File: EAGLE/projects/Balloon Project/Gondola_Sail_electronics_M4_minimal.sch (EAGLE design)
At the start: 38 parts

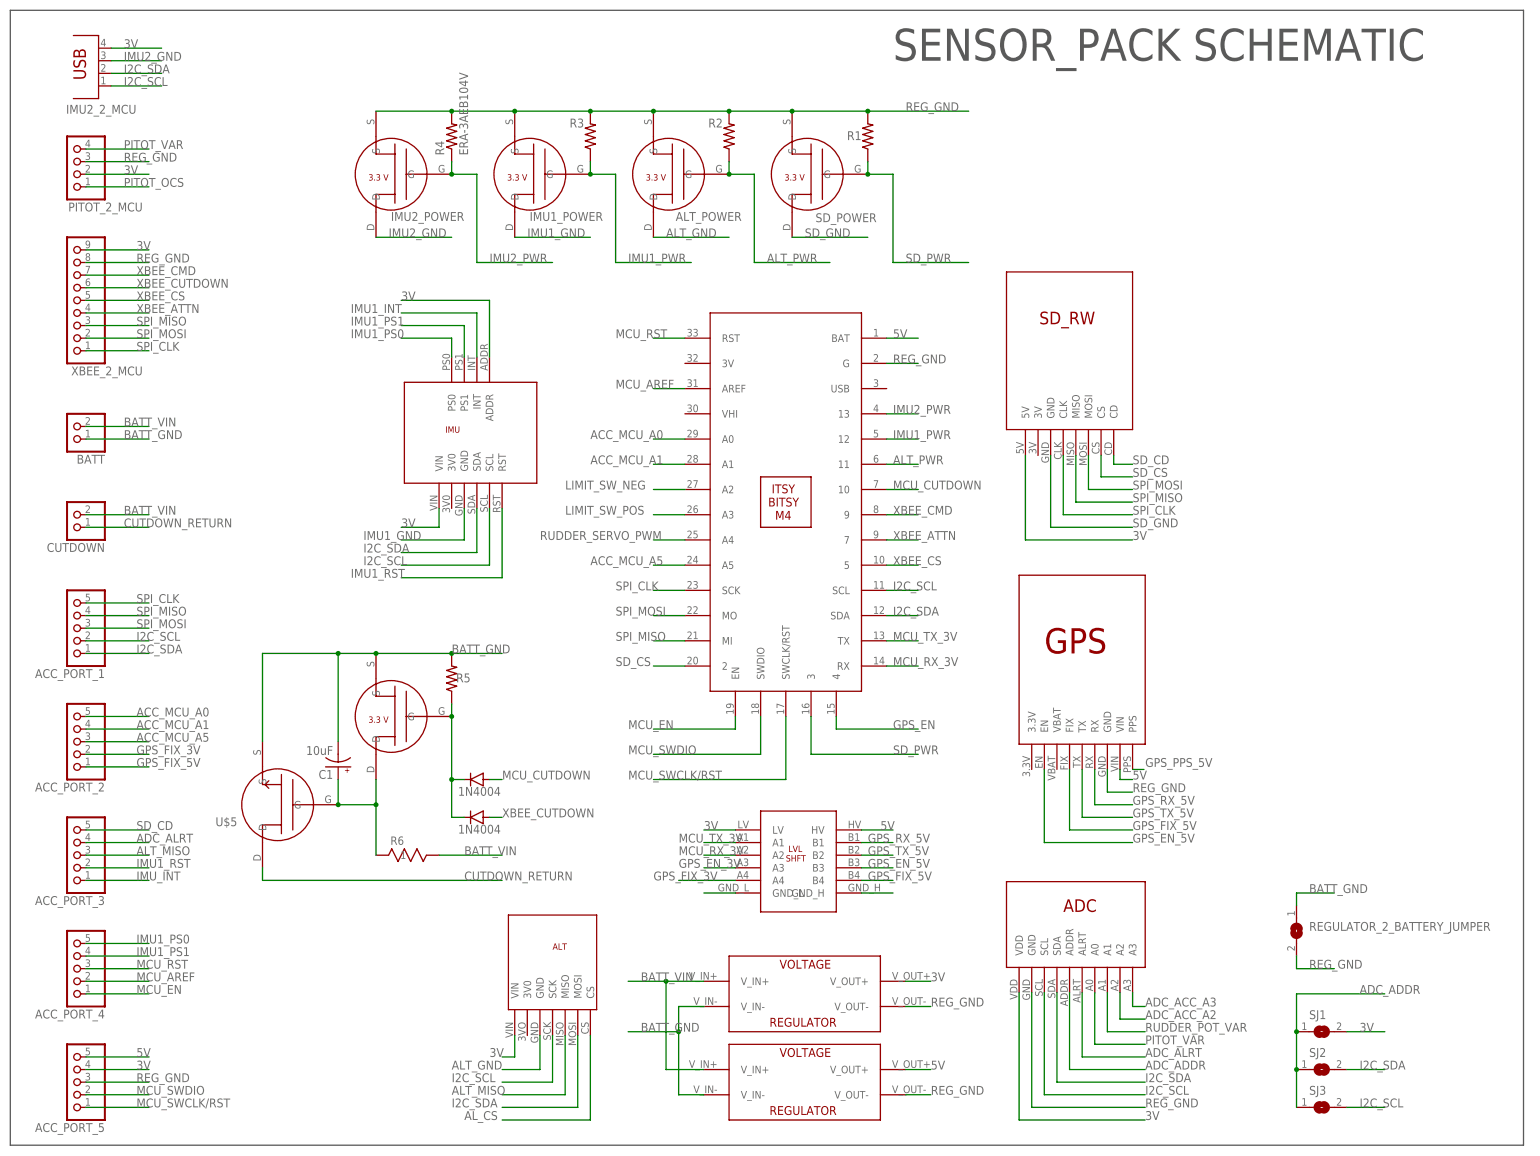
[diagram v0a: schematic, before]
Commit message: added minimal sensorpack
full sensor pack has too many breakout pins, need to trim down the size of the board. starting routing traces
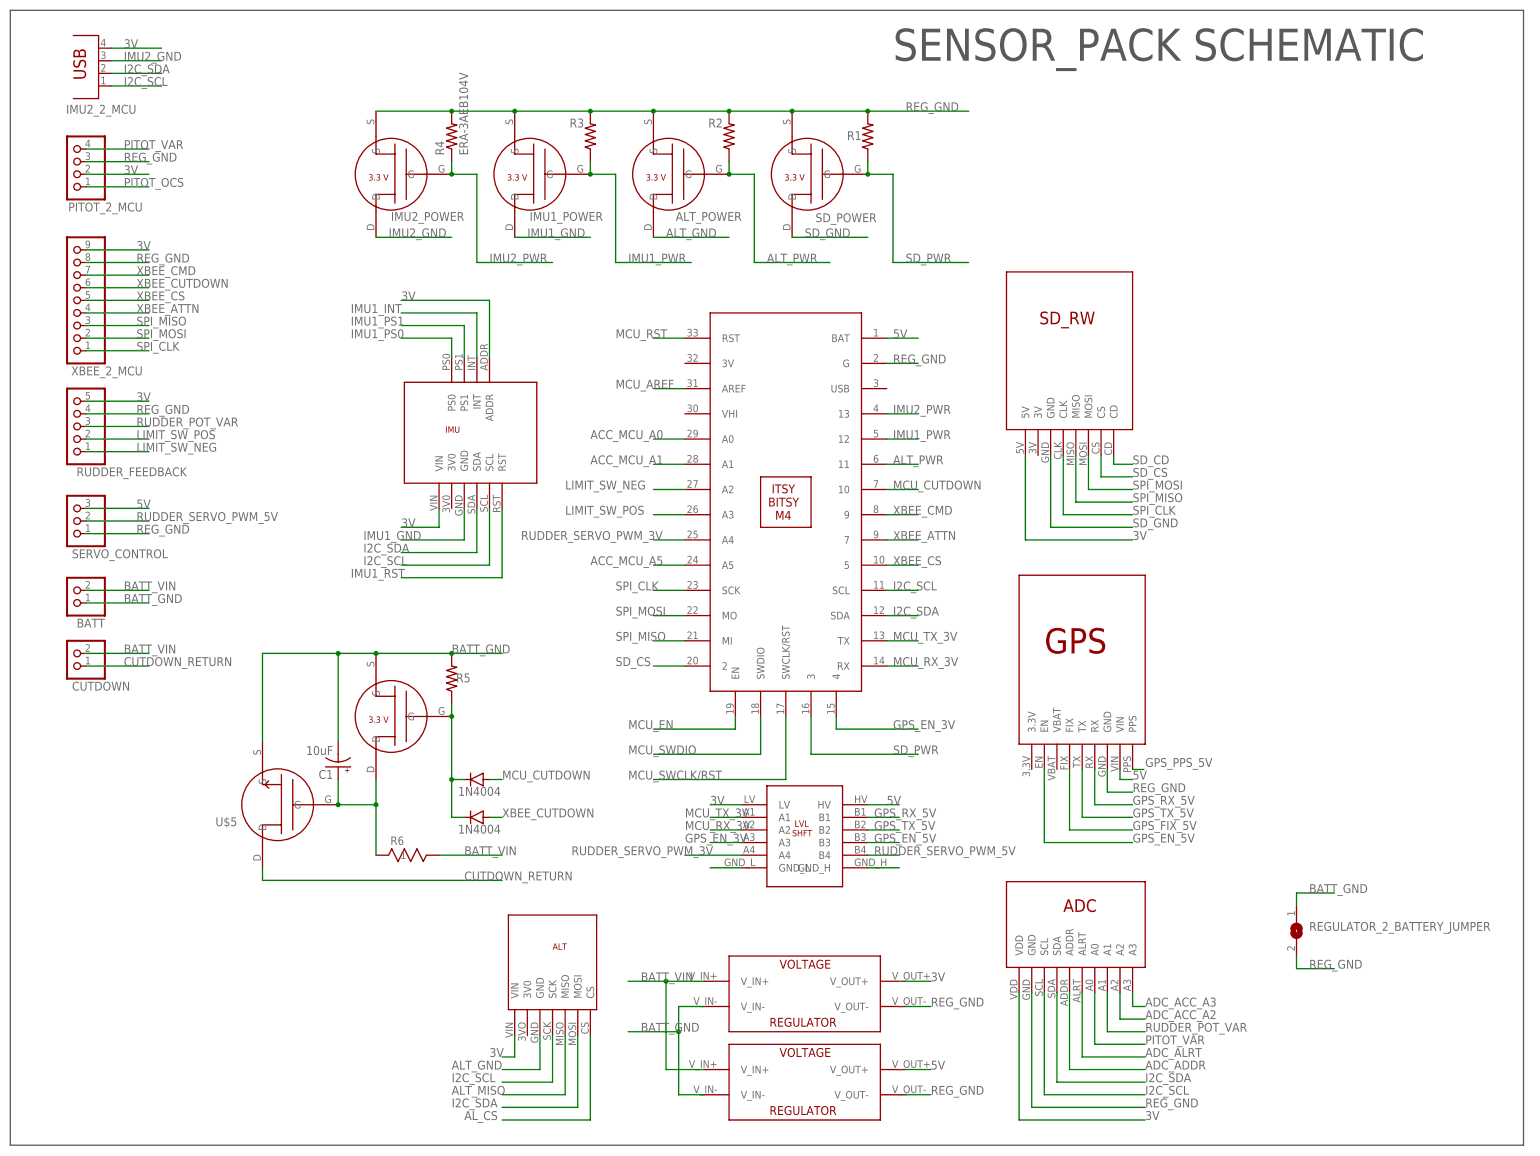
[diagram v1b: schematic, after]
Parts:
- removed ACC_PORT_1, ACC_PORT_2, ACC_PORT_3, ACC_PORT_4, ACC_PORT_5: (no value), pinhead:PINHD-1X5/90
- removed SJ1, SJ2, SJ3: (no value), jumper:SJ
- added RUDDER_FEEDBACK: (no value), pinhead:PINHD-1X5/90
- added SERVO_CONTROL: (no value), pinhead:PINHD-1X3/90
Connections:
- removed net GPS_EN: U$8.4
- removed net GPS_FIX_3V: ACC_PORT_2.2, U$6.A4
- removed net IMU_INT: ACC_PORT_3.1
- removed net RUDDER_SERVO_PWM: U$8.A4
- new net RUDDER_SERVO_PWM_3V: U$6.A4, U$8.A4
- new net RUDDER_SERVO_PWM_5V: SERVO_CONTROL.2, U$6.B4
- net 3V: now also RUDDER_FEEDBACK.5; no longer ACC_PORT_5.4, SJ1.2
- net 5V: now also SERVO_CONTROL.3; no longer ACC_PORT_5.5
- net ACC_MCU_A0: no longer ACC_PORT_2.5
- net ACC_MCU_A1: no longer ACC_PORT_2.4
- net ACC_MCU_A5: no longer ACC_PORT_2.3
- net ADC_ADDR: no longer SJ1.1, SJ2.1, SJ3.1
- net ADC_ALRT: no longer ACC_PORT_3.4
- net ALT_MISO: no longer ACC_PORT_3.3
- net GPS_EN_3V: now also U$8.4
- net GPS_FIX_5V: no longer ACC_PORT_2.1, U$6.B4
- net I2C_SCL: no longer ACC_PORT_1.2, SJ3.2
- net I2C_SDA: no longer ACC_PORT_1.1, SJ2.2
- net IMU1_PS0: no longer ACC_PORT_4.5
- net IMU1_PS1: no longer ACC_PORT_4.4
- net IMU1_RST: no longer ACC_PORT_3.2
- net LIMIT_SW_NEG: now also RUDDER_FEEDBACK.1
- net LIMIT_SW_POS: now also RUDDER_FEEDBACK.2
- net MCU_AREF: no longer ACC_PORT_4.2
- net MCU_EN: no longer ACC_PORT_4.1
- net MCU_RST: no longer ACC_PORT_4.3
- net MCU_SWCLK/RST: no longer ACC_PORT_5.1
- net MCU_SWDIO: no longer ACC_PORT_5.2
- net REG_GND: now also RUDDER_FEEDBACK.4, SERVO_CONTROL.1; no longer ACC_PORT_5.3
- net RUDDER_POT_VAR: now also RUDDER_FEEDBACK.3
- net SD_CD: no longer ACC_PORT_3.5
- net SPI_CLK: no longer ACC_PORT_1.5
- net SPI_MISO: no longer ACC_PORT_1.4
- net SPI_MOSI: no longer ACC_PORT_1.3
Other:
- moved on the sheet: BATT, CUTDOWN

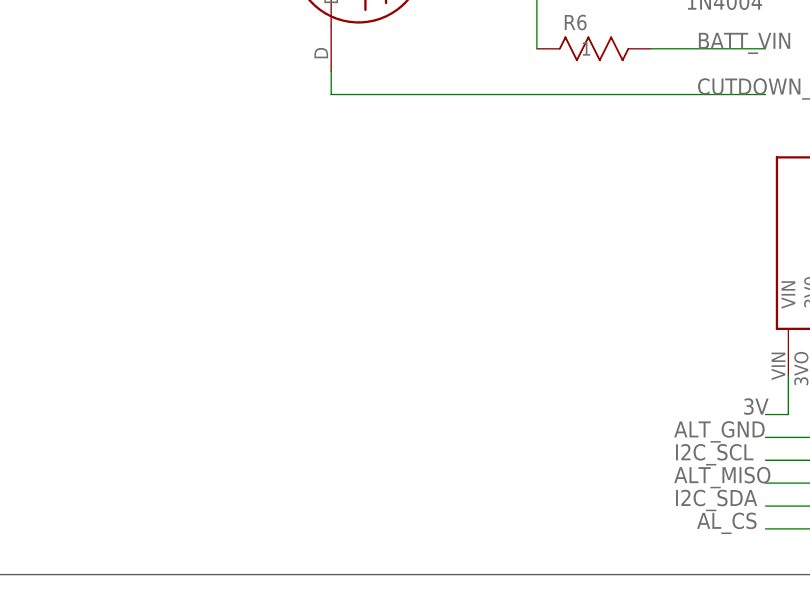
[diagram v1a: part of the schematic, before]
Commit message: minimal telemetry/sensor board complete
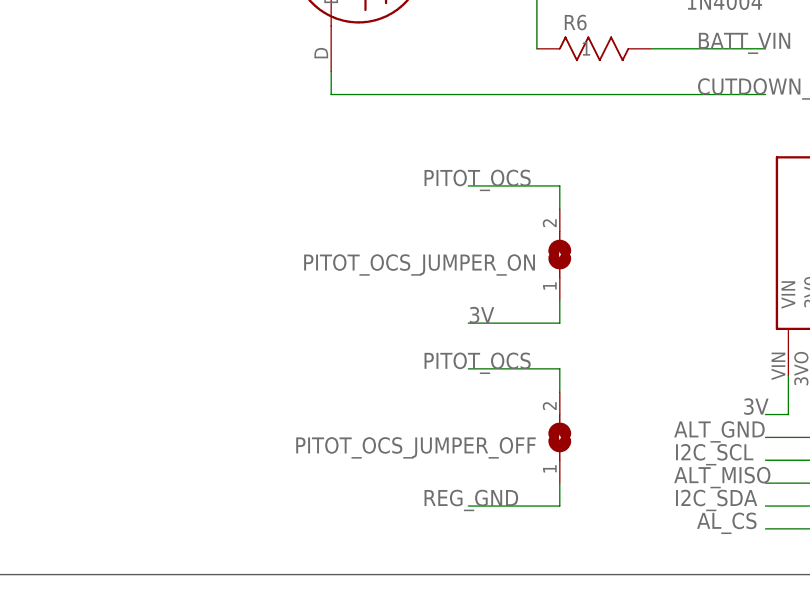
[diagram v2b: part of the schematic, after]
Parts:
- added PITOT_OCS_JUMPER_OFF, PITOT_OCS_JUMPER_ON: (no value), jumper:SJ
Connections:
- net 3V: now also PITOT_OCS_JUMPER_ON.1
- net PITOT_OCS: now also PITOT_OCS_JUMPER_OFF.2, PITOT_OCS_JUMPER_ON.2
- net REG_GND: now also PITOT_OCS_JUMPER_OFF.1
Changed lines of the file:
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@@
 <?xml version="1.0" encoding="utf-8"?>
 <!DOCTYPE eagle SYSTEM "eagle.dtd">
-<eagle version="9.3.0">
+<eagle version="9.4.2">
 <drawing>
 <settings>
@@
 <part name="RUDDER_FEEDBACK" library="pinhead" library_urn="urn:adsk.eagle:library:325" deviceset="PINHD-1X5" device="/90" package3d_urn="urn:adsk.eagle:package:22467/2"/>
 <part name="SERVO_CONTROL" library="pinhead" library_urn="urn:adsk.eagle:library:325" deviceset="PINHD-1X3" device="/90" package3d_urn="urn:adsk.eagle:package:22459/2"/>
+<part name="PITOT_OCS_JUMPER_ON" library="jumper" library_urn="urn:adsk.eagle:library:252" deviceset="SJ" device="" package3d_urn="urn:adsk.eagle:package:15471/1"/>
+<part name="PITOT_OCS_JUMPER_OFF" library="jumper" library_urn="urn:adsk.eagle:library:252" deviceset="SJ" device="" package3d_urn="urn:adsk.eagle:package:15471/1"/>
 </parts>
 <sheets>
@@
 <attribute name="VALUE" x="19.05" y="133.35" size="1.778" layer="96" rot="R180"/>
 </instance>
+<instance part="PITOT_OCS_JUMPER_ON" gate="1" x="76.2" y="35.56" smashed="yes" rot="R90">
+<attribute name="NAME" x="73.66" y="35.56" size="1.778" layer="95" rot="R180"/>
+<attribute name="VALUE" x="80.01" y="33.02" size="1.778" layer="96" rot="R90"/>
+</instance>
+<instance part="PITOT_OCS_JUMPER_OFF" gate="1" x="76.2" y="15.24" smashed="yes" rot="R90">
+<attribute name="NAME" x="73.66" y="15.24" size="1.778" layer="95" rot="R180"/>
+<attribute name="VALUE" x="80.01" y="12.7" size="1.778" layer="96" rot="R90"/>
+</instance>
 </instances>
 <busses>
@@
 <wire x1="15.24" y1="149.86" x2="27.94" y2="149.86" width="0.1524" layer="91"/>
 <label x="25.4" y="149.86" size="1.778" layer="95"/>
+</segment>
+<segment>
+<pinref part="PITOT_OCS_JUMPER_ON" gate="1" pin="1"/>
+<wire x1="76.2" y1="30.48" x2="76.2" y2="27.94" width="0.1524" layer="91"/>
+<wire x1="76.2" y1="27.94" x2="66.04" y2="27.94" width="0.1524" layer="91"/>
+<label x="66.04" y="27.94" size="1.778" layer="95"/>
 </segment>
 </net>
@@
 <label x="25.4" y="147.32" size="1.778" layer="95"/>
 </segment>
+<segment>
+<pinref part="PITOT_OCS_JUMPER_OFF" gate="1" pin="1"/>
+<wire x1="76.2" y1="10.16" x2="76.2" y2="7.62" width="0.1524" layer="91"/>
+<wire x1="76.2" y1="7.62" x2="66.04" y2="7.62" width="0.1524" layer="91"/>
+<label x="60.96" y="7.62" size="1.778" layer="95"/>
+</segment>
 </net>
 <net name="MCU_TX_3V" class="0">
@@
 <label x="22.86" y="193.04" size="1.778" layer="95"/>
 </segment>
-</net>
+<segment>
+<pinref part="PITOT_OCS_JUMPER_ON" gate="1" pin="2"/>
+<wire x1="76.2" y1="40.64" x2="76.2" y2="43.18" width="0.1524" layer="91"/>
+<wire x1="76.2" y1="43.18" x2="66.04" y2="43.18" width="0.1524" layer="91"/>
+<label x="60.96" y="43.18" size="1.778" layer="95"/>
+</segment>
+<segment>
+<pinref part="PITOT_OCS_JUMPER_OFF" gate="1" pin="2"/>
+<wire x1="76.2" y1="20.32" x2="76.2" y2="22.86" width="0.1524" layer="91"/>
+<wire x1="76.2" y1="22.86" x2="66.04" y2="22.86" width="0.1524" layer="91"/>
+<label x="60.96" y="22.86" size="1.778" layer="95"/>
+</segment>
+</net>
